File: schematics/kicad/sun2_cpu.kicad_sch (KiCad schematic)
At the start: 22 parts, among them U100 MC68010, U102 74F00, U109 74F08, U110 7407, U111 74F251, U114 74LS20, U115 74F04, U119 74LS148, U120 8211, U122 7406, U206 74F74, U608 74LS04, U610 74LS04

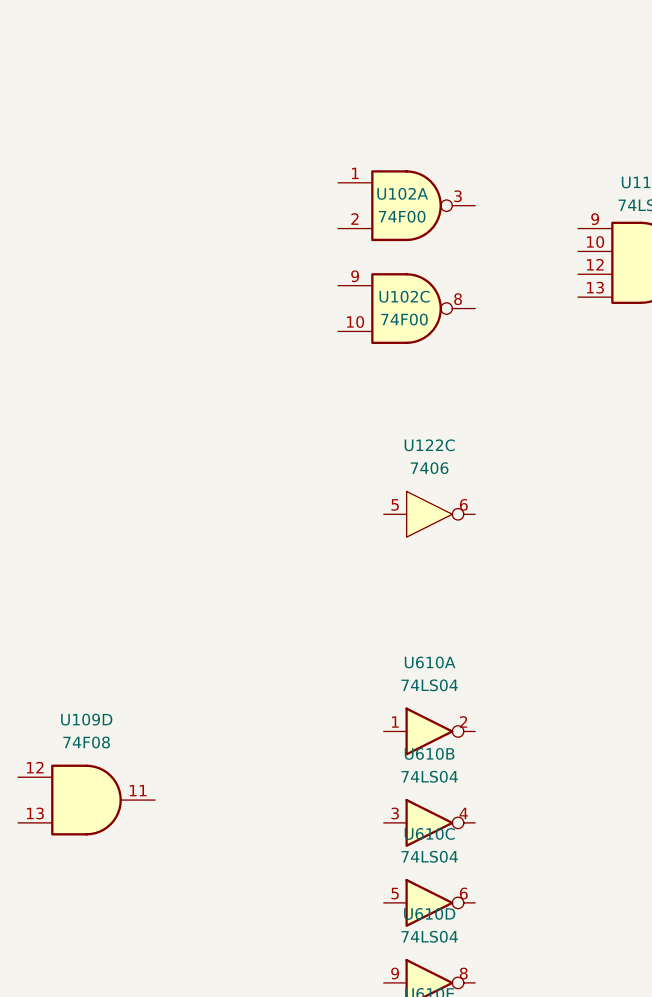
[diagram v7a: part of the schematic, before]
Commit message: Start on rasterop, parity, P2
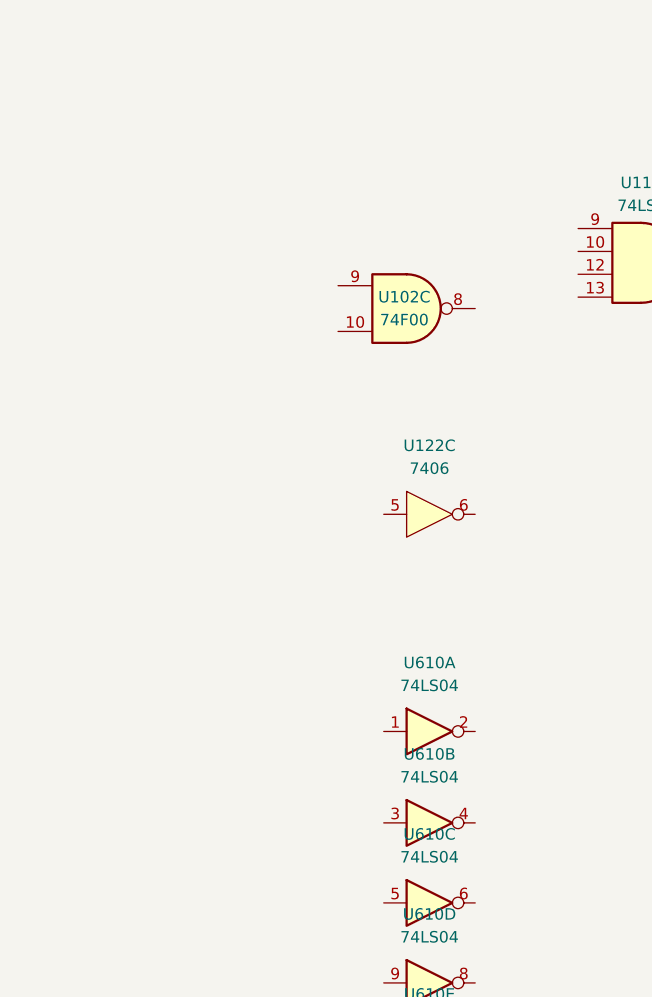
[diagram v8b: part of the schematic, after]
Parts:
- removed unit 1 of U102
- removed unit 4 of U109
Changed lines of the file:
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@@
 	)
 	(symbol
-		(lib_id "sun2:74F08")
-		(at -68.58 120.65 0)
-		(unit 4)
-		(exclude_from_sim no)
-		(in_bom yes)
-		(on_board yes)
-		(dnp no)
-		(fields_autoplaced yes)
-		(property "Reference" "U109"
-			(at -68.5883 111.76 0)
-			(effects
-				(font
-					(size 1.27 1.27)
-				)
-			)
-		)
-		(property "Value" "74F08"
-			(at -68.5883 114.3 0)
-			(effects
-				(font
-					(size 1.27 1.27)
-				)
-			)
-		)
-		(property "Footprint" "Package_DIP:DIP-14_W7.62mm"
-			(at -68.58 120.65 0)
-			(effects
-				(font
-					(size 1.27 1.27)
-				)
-				(hide yes)
-			)
-		)
-		(property "Datasheet" "https://www.ti.com/lit/ds/symlink/sn74f08.pdf"
-			(at -68.58 120.65 0)
-			(effects
-				(font
-					(size 1.27 1.27)
-				)
-				(hide yes)
-			)
-		)
-		(property "Description" "Quad And2"
-			(at -68.58 120.65 0)
-			(effects
-				(font
-					(size 1.27 1.27)
-				)
-				(hide yes)
-			)
-		)
-		(property "Order Link" "https://www.digikey.com/en/products/detail/texas-instruments/SN74F08N/373669"
-			(at -68.58 120.65 0)
-			(effects
-				(font
-					(size 1.27 1.27)
-				)
-				(hide yes)
-			)
-		)
-		(pin "7"
-		)
-		(pin "5"
-		)
-		(pin "4"
-		)
-		(pin "10"
-		)
-		(pin "11"
-		)
-		(pin "13"
-		)
-		(pin "12"
-		)
-		(pin "8"
-		)
-		(pin "6"
-		)
-		(pin "14"
-		)
-		(pin "9"
-		)
-		(pin "2"
-		)
-		(pin "1"
-		)
-		(pin "3"
-		)
-		(instances
-			(project ""
-				(path "/67ee2072-0b57-4a50-8537-b17b5f651e89/2d3d381d-4c8b-4bfc-8adc-91fc2fe1e9d0"
-					(reference "U109")
-					(unit 4)
-				)
-			)
-		)
-	)
-	(symbol
 		(lib_id "sun2:74LS148")
 		(at 107.95 161.29 0)
@@
 					(unit 1)
 				)
-			)
-		)
-	)
-	(symbol
-		(lib_id "sun2:74F00")
-		(at -33.02 54.61 0)
-		(unit 1)
-		(exclude_from_sim no)
-		(in_bom yes)
-		(on_board yes)
-		(dnp no)
-		(property "Reference" "U102"
-			(at -33.528 53.34 0)
-			(effects
-				(font
-					(size 1.27 1.27)
-				)
-			)
-		)
-		(property "Value" "74F00"
-			(at -33.528 55.88 0)
-			(effects
-				(font
-					(size 1.27 1.27)
-				)
-			)
-		)
-		(property "Footprint" "Package_DIP:DIP-14_W7.62mm"
-			(at -33.02 54.61 0)
-			(effects
-				(font
-					(size 1.27 1.27)
-				)
-				(hide yes)
-			)
-		)
-		(property "Datasheet" "https://www.ti.com/lit/ds/symlink/sn74f00.pdf"
-			(at -33.02 54.61 0)
-			(effects
-				(font
-					(size 1.27 1.27)
-				)
-				(hide yes)
-			)
-		)
-		(property "Description" "quad 2-input NAND gate"
-			(at -33.02 54.61 0)
-			(effects
-				(font
-					(size 1.27 1.27)
-				)
-				(hide yes)
-			)
-		)
-		(property "Order Link" "https://www.digikey.com/en/products/detail/texas-instruments/SN74F00N/373665"
-			(at -33.02 54.61 0)
-			(effects
-				(font
-					(size 1.27 1.27)
-				)
-				(hide yes)
-			)
-		)
-		(pin "4"
-		)
-		(pin "9"
-		)
-		(pin "5"
-		)
-		(pin "6"
-		)
-		(pin "13"
-		)
-		(pin "11"
-		)
-		(pin "3"
-		)
-		(pin "1"
-		)
-		(pin "2"
-		)
-		(pin "12"
-		)
-		(pin "10"
-		)
-		(pin "8"
-		)
-		(pin "14"
-		)
-		(pin "7"
-		)
-		(instances
-			(project ""
-				(path "/67ee2072-0b57-4a50-8537-b17b5f651e89/2d3d381d-4c8b-4bfc-8adc-91fc2fe1e9d0"
-					(reference "U102")
-					(unit 1)
-				)
